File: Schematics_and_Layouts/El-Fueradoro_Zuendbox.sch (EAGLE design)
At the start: 140 parts, among them IC1 MAX202, IC2 MEGA168P/328P, IC4 MC33063-DIL, IC6 74HC595N, IC7 74HC595N, IC8 LD117AV, Q1 9.8304, Q10 IRF3708, Q11 IRF3708, Q12 IRF3708, Q13 IRF3708, Q14 IRF3708, Q15 IRF3708, Q16 IRF3708, Q17 IRF3708, Q2 IRF3708, Q3 IRF3708, Q4 IRF3708, Q5 IRF3708, Q6 IRF3708, Q7 IRF3708, Q8 IRF3708, Q9 IRF3708

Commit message: Added size-information-output for Hexfiles/build_hexfiles.bat Extended manual and added BOMs BOM-Update (final one, hopefully!)
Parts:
- R12, R38: value 4k7 -> 3k3
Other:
- moved on the sheet: BATT_IN, C13, C18, C19, C20, C21, C22, C23, C24, C25, C26, C27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

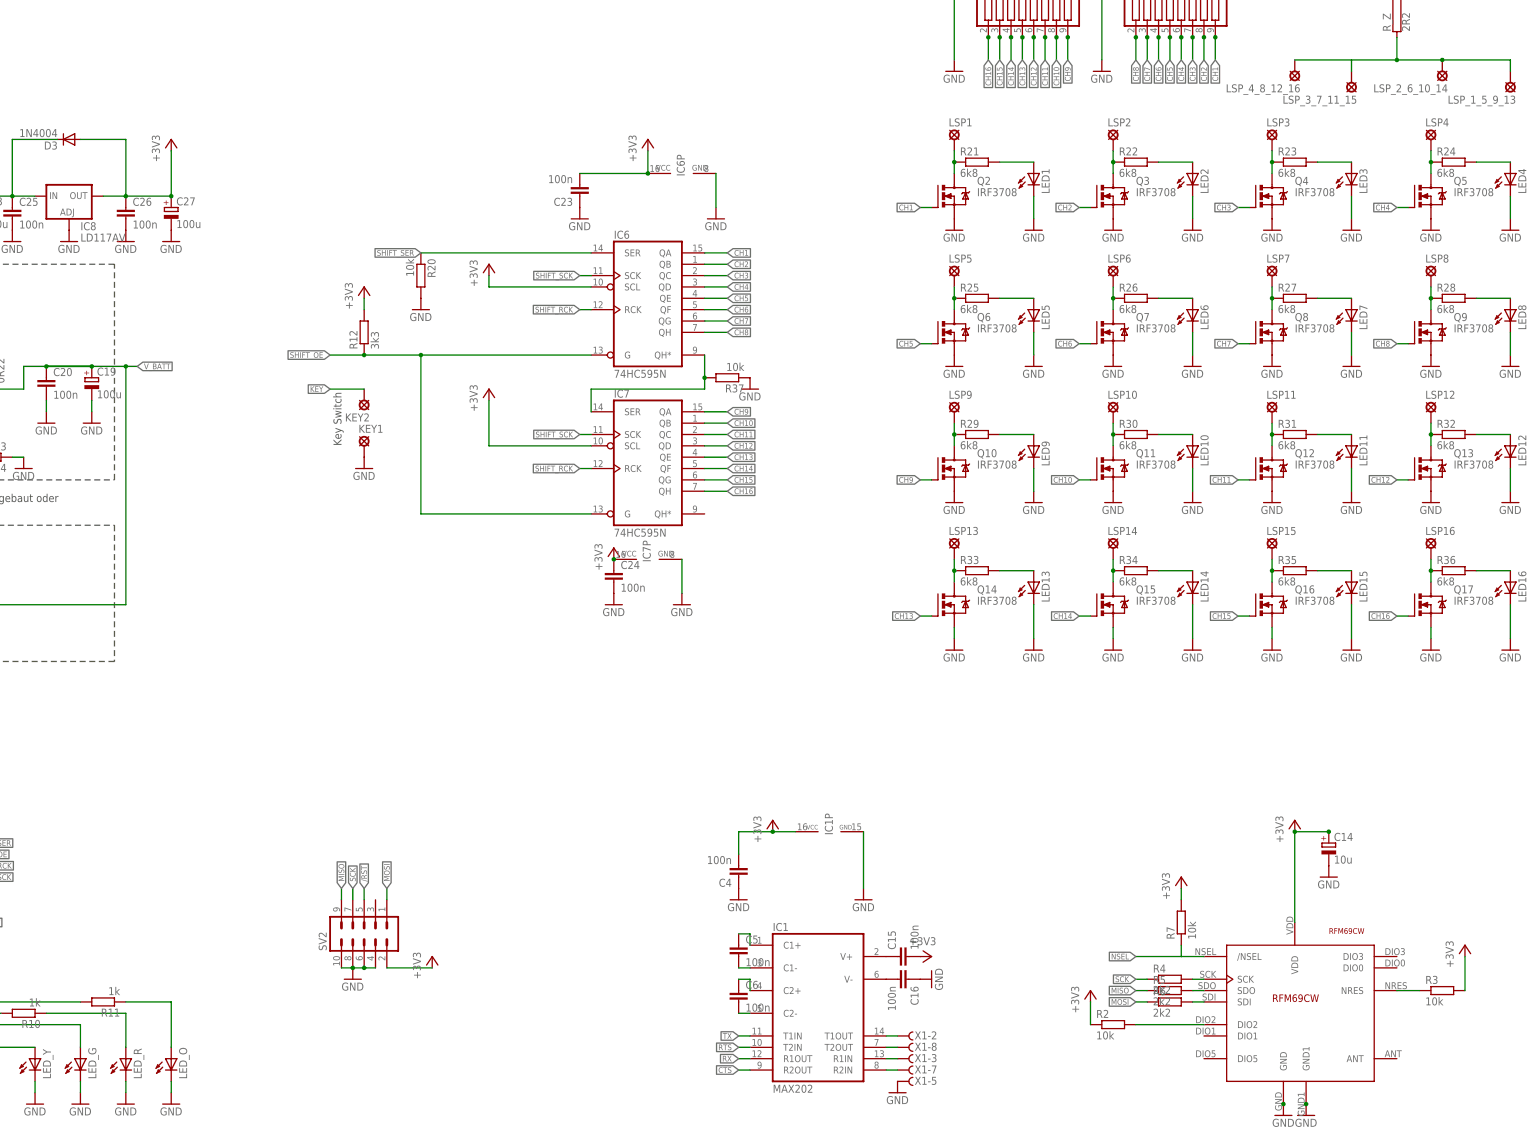
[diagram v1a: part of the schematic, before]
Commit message: Layout fixes Additions to manual once again
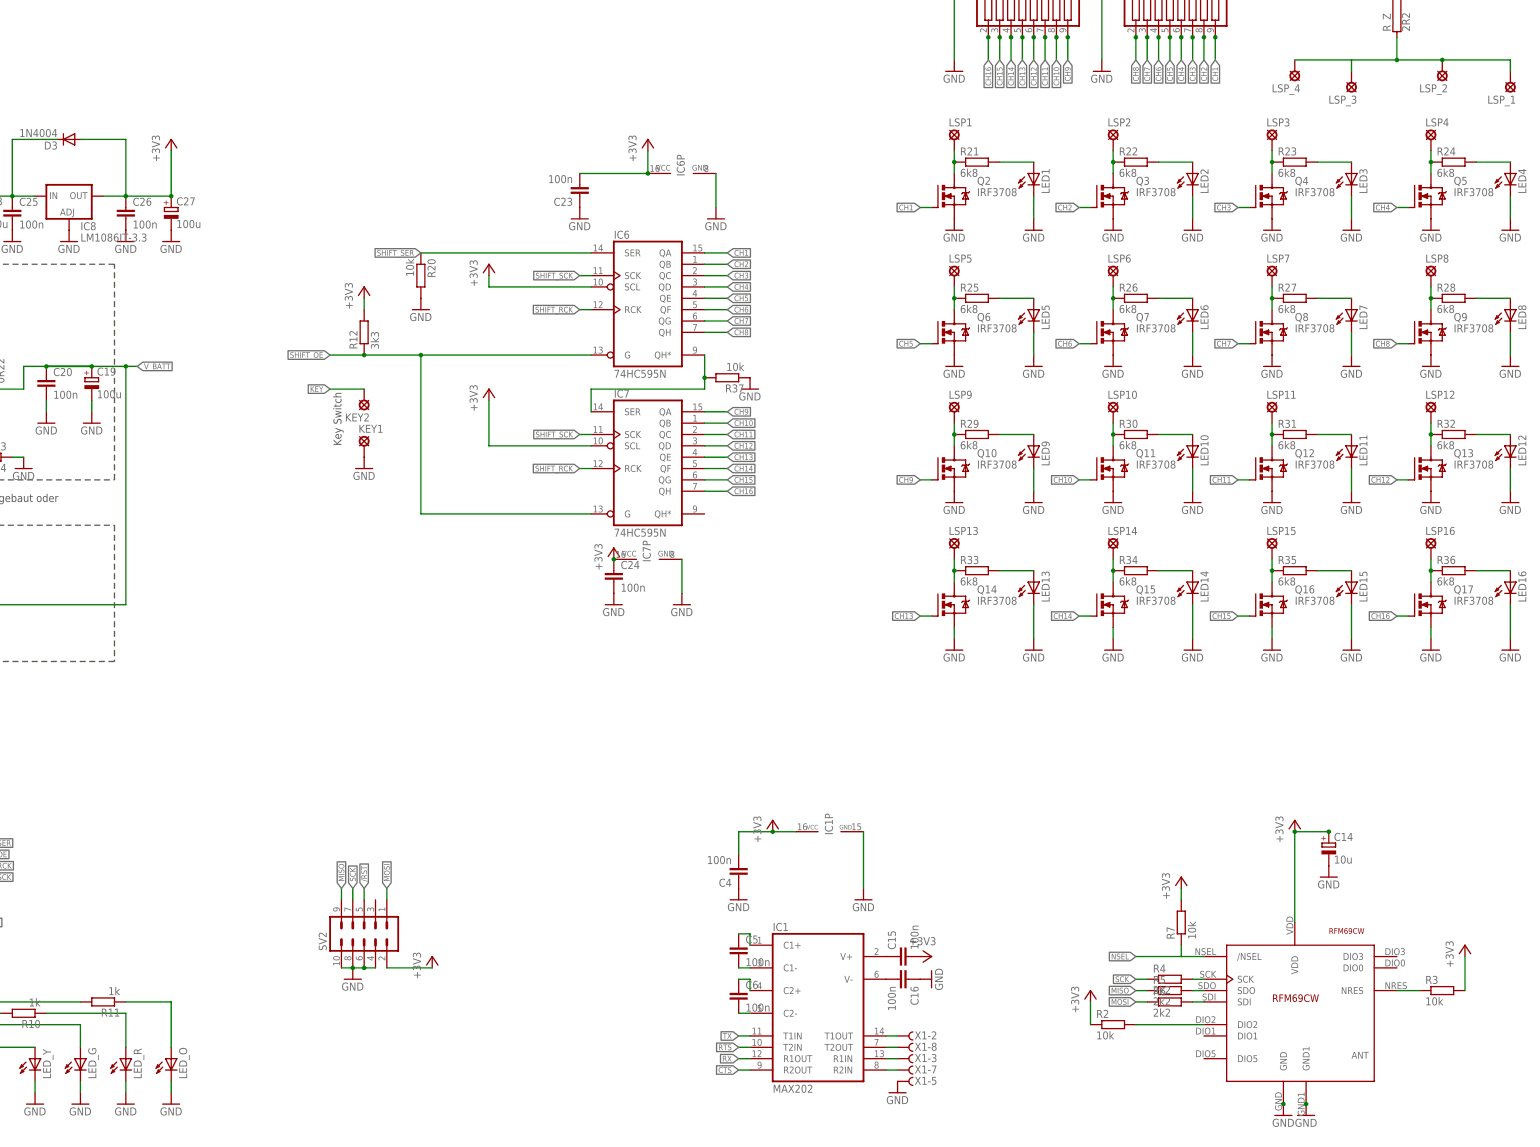
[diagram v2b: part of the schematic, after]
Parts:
- IC8: value LD117AV -> LM1086IT-3.3
- renumbered LSP_1_5_9_13 to LSP_1, LSP_2_6_10_14 to LSP_2, LSP_3_7_11_15 to LSP_3, LSP_4_8_12_16 to LSP_4
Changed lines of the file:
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@@
 <part name="GND46" library="supply1" deviceset="GND" device=""/>
 <part name="GND47" library="supply1" deviceset="GND" device=""/>
-<part name="LSP_4_8_12_16" library="solpad" deviceset="LSP11" device=""/>
-<part name="LSP_3_7_11_15" library="solpad" deviceset="LSP11" device=""/>
-<part name="LSP_2_6_10_14" library="solpad" deviceset="LSP11" device=""/>
-<part name="LSP_1_5_9_13" library="solpad" deviceset="LSP11" device=""/>
+<part name="LSP_4" library="solpad" deviceset="LSP11" device=""/>
+<part name="LSP_3" library="solpad" deviceset="LSP11" device=""/>
+<part name="LSP_2" library="solpad" deviceset="LSP11" device=""/>
+<part name="LSP_1" library="solpad" deviceset="LSP11" device=""/>
 <part name="C21" library="rcl" deviceset="CPOL-EU" device="E7.5-18" value="4700u"/>
 <part name="C22" library="rcl" deviceset="CPOL-EU" device="E7.5-18" value="4700u"/>
@@
 <part name="GND79" library="supply1" deviceset="GND" device=""/>
 <part name="+3V2" library="supply1" deviceset="+3V3" device=""/>
-<part name="IC8" library="v-reg" deviceset="LD117A?*" device="V" value="LD117AV"/>
+<part name="IC8" library="v-reg" deviceset="LD117A?*" device="V" value="LM1086IT-3.3"/>
 <part name="+3V3" library="supply1" deviceset="+3V3" device=""/>
 <part name="+3V4" library="supply1" deviceset="+3V3" device=""/>
@@
 <instance part="GND46" gate="1" x="447.04" y="111.76"/>
 <instance part="GND47" gate="1" x="447.04" y="144.78"/>
-<instance part="LSP_4_8_12_16" gate="1" x="416.56" y="241.3" rot="R180"/>
-<instance part="LSP_3_7_11_15" gate="1" x="429.26" y="238.76" rot="R180"/>
-<instance part="LSP_2_6_10_14" gate="1" x="449.58" y="241.3" rot="R180"/>
-<instance part="LSP_1_5_9_13" gate="1" x="464.82" y="238.76" rot="R180"/>
+<instance part="LSP_4" gate="1" x="416.56" y="241.3" rot="R180"/>
+<instance part="LSP_3" gate="1" x="429.26" y="238.76" rot="R180"/>
+<instance part="LSP_2" gate="1" x="449.58" y="241.3" rot="R180"/>
+<instance part="LSP_1" gate="1" x="464.82" y="238.76" rot="R180"/>
 <instance part="C21" gate="G$1" x="20.32" y="182.88"/>
 <instance part="C22" gate="G$1" x="30.48" y="182.88"/>
@@
 <net name="N$35" class="0">
 <segment>
-<pinref part="LSP_2_6_10_14" gate="1" pin="MP"/>
-<pinref part="LSP_1_5_9_13" gate="1" pin="MP"/>
+<pinref part="LSP_2" gate="1" pin="MP"/>
+<pinref part="LSP_1" gate="1" pin="MP"/>
 <wire x1="464.82" y1="241.3" x2="464.82" y2="243.84" width="0.1524" layer="91"/>
 <wire x1="464.82" y1="243.84" x2="449.58" y2="243.84" width="0.1524" layer="91"/>
 <junction x="449.58" y="243.84"/>
-<pinref part="LSP_3_7_11_15" gate="1" pin="MP"/>
+<pinref part="LSP_3" gate="1" pin="MP"/>
 <wire x1="429.26" y1="243.84" x2="439.42" y2="243.84" width="0.1524" layer="91"/>
 <wire x1="439.42" y1="243.84" x2="449.58" y2="243.84" width="0.1524" layer="91"/>
 <wire x1="429.26" y1="241.3" x2="429.26" y2="243.84" width="0.1524" layer="91"/>
 <wire x1="429.26" y1="243.84" x2="416.56" y2="243.84" width="0.1524" layer="91"/>
-<pinref part="LSP_4_8_12_16" gate="1" pin="MP"/>
+<pinref part="LSP_4" gate="1" pin="MP"/>
 <pinref part="R_Z" gate="G$1" pin="1"/>
 <wire x1="439.42" y1="248.92" x2="439.42" y2="243.84" width="0.1524" layer="91"/>
